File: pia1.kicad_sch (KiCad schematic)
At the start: 33 parts, among them IC20 MC14529B, IC24 74LS244N, IC25 LM393P, IC26 MC6821

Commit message: move to samx4
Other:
- company: (none) -> Dragon Data
- title: (none) -> Dragon 32 CPU UK PAL
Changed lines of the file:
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@@
   (paper "A3")
   (title_block
+    (title "Dragon 32 CPU UK PAL")
     (date "2023-05-25")
     (rev "3.0")
-    (comment 2 "Reposition dram and buffer")
+    (company "Dragon Data")
+    (comment 1 "Modified by Julian Brown")
+    (comment 2 "SAMx4 by Ciaran Anscomb")
   )
   (junction (at 89.281 73.406) (diameter 0) (color 0 0 0 0)

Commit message: rework board
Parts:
- removed IC26: MC6821, Package_DIP:DIP-40_W15.24mm, symbol Motorola PIA:MC6821
- added U5: W65C21, Package_LCC:PLCC-44_SMD-Socket, symbol Motorola PIA:W65C21
- C1, C38, C39, C43, C45, C68, C69: footprint Capacitor_THT:C_Disc_D4.3mm_W1.9mm_P5.00mm -> Capacitor_SMD:C_0805_2012Metric_Pad1.18x1.45mm_HandSolder
- C30, C31, C32, C33: footprint Capacitor_THT:C_Disc_D5.0mm_W2.5mm_P5.00mm -> Capacitor_SMD:C_0805_2012Metric_Pad1.18x1.45mm_HandSolder
- D8, D9: footprint Diode_THT:D_DO-35_SOD27_P7.62mm_Horizontal -> Diode_SMD:D_SOD-323_HandSoldering
- IC24: value 74LS244N -> 74ACT244N; footprint Package_DIP:DIP-20_W7.62mm -> Package_SO:SOIC-20W_7.5x12.8mm_P1.27mm; DigiKey 296-1653-5-ND -> 74ACT244SCXCT-ND
- L1, L2, L3, L4: footprint Inductor_THT:L_Axial_L7.0mm_D3.3mm_P5.08mm_Vertical_Fastron_MICC -> Inductor_SMD:L_1812_4532Metric_Pad1.30x3.40mm_HandSolder
- R1, R42, R43, R53, R54, R55: footprint Resistor_THT:R_Axial_DIN0207_L6.3mm_D2.5mm_P10.16mm_Horizontal -> Resistor_SMD:R_0805_2012Metric_Pad1.20x1.40mm_HandSolder
- R30, R31: footprint Resistor_THT:R_Axial_DIN0207_L6.3mm_D2.5mm_P2.54mm_Vertical -> Resistor_SMD:R_0805_2012Metric_Pad1.20x1.40mm_HandSolder
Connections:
- net +5V: now also U5.21 (VCC), U5.24 (CS0), U5.26 (CS1)
- net A0: now also U5.39 (RS0)
- net A1: now also U5.38 (RS1)
- net AD1: now also U5.43 (CA2)
- net AD2: now also U5.20 (CB2)
- net D0: now also U5.36 (D0)
- net D1: now also U5.35 (D1)
- net D2: now also U5.34 (D2)
- net D3: now also U5.33 (D3)
- net D4: now also U5.32 (D4)
- net D5: now also U5.31 (D5)
- net D6: now also U5.30 (D6)
- net D7: now also U5.29 (D7)
- net E: now also U5.28 (E)
- net GND: now also U5.1 (VSS)
- net P0: now also U5.25 (~{CS2})
- net PA0: now also U5.3 (PA0)
- net PA1: now also U5.4 (PA1)
- net PA2: now also U5.5 (PA2)
- net PA3: now also U5.6 (PA3)
- net PA4: now also U5.7 (PA4)
- net PA5: now also U5.8 (PA5)
- net PA6: now also U5.9 (PA6)
- net PA7: now also U5.10 (PA7)
- net PB0: now also U5.11 (PB0)
- net PB1: now also U5.12 (PB1)
- net PB2: now also U5.13 (PB2)
- net PB3: now also U5.14 (PB3)
- net PB4: now also U5.15 (PB4)
- net PB5: now also U5.16 (PB5)
- net PB6: now also U5.17 (PB6)
- net PB7: now also U5.18 (PB7)
- net R/~{W}: now also U5.23 (R/~{W})
- net ~{FS}: now also U5.19 (CB1)
- net ~{IRQ}: now also U5.41 (~{IRQB}), U5.42 (~{IRQA})
- net ~{NHS}: now also U5.44 (CA1)
- net ~{RES}: now also U5.37 (~{RESET})

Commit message: serial wiring
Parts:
- removed IC20: MC14529B, Package_DIP:DIP-16_W7.62mm, symbol Motorola PIA:MC14529B
- removed IC25: LM393P, Package_DIP:DIP-8_W7.62mm, symbol Comparator:LM393
- removed R53: 10M, Resistor_SMD:R_0805_2012Metric_Pad1.20x1.40mm_HandSolder, symbol Device:R_Small
- removed R54: 1K, Resistor_SMD:R_0805_2012Metric_Pad1.20x1.40mm_HandSolder, symbol Device:R_Small
- removed R55: 10K, Resistor_SMD:R_0805_2012Metric_Pad1.20x1.40mm_HandSolder, symbol Device:R_Small
- added IC1: LM393DR, Package_SO:SOP-8_3.9x4.9mm_P1.27mm, symbol Comparator:LM393
- added JP3: Serial, Jumper:SolderJumper-3_P1.3mm_Open_Pad1.0x1.5mm, symbol Jumper:SolderJumper_3_Open
- added R28: 4K7, Resistor_SMD:R_0805_2012Metric_Pad1.20x1.40mm_HandSolder, symbol Device:R_Small
- added R33: 10M, Resistor_SMD:R_0805_2012Metric_Pad1.20x1.40mm_HandSolder, symbol Device:R_Small
- added R34: 1K, Resistor_SMD:R_0805_2012Metric_Pad1.20x1.40mm_HandSolder, symbol Device:R_Small
- added U1: TS5A3166DBVR, Package_TO_SOT_SMD:SOT-23-5, symbol Analog_Switch:TS5A3166DBVR
- added U13: 4069, Package_SO:SOIC-14_3.9x8.7mm_P1.27mm, symbol 4xxx:4069
- added U2: 4052, Package_SO:TSSOP-16_4.4x5mm_P0.65mm, symbol 4xxx:4052
- R31: value 4K7 -> 10K; DigiKey CF14JT4K70CT-ND -> CF14JT10K0CT-ND
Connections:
- net +5V: now also JP3.3 (B), R28.2, R34.1, U1.5 (V+), U2.16 (VDD); no longer R31.2, U5.24 (CS0), U5.26 (CS1)
- net 6bit D/A: now also IC1.6 (_), U2.1 (Y0)
- net AD1: now also U2.10 (A)
- net AD2: now also U2.9 (B)
- net CASS: now also R28.1, U2.5 (Y1); no longer R31.1
- net CB2: now also U1.4
- net ESND: now also U2.2 (Y2)
- net GND: now also U1.3 (GND), U2.4 (Y3), U2.6 (Inh), U2.7 (VEE), U2.8 (VSS)
- net PA7: now also IC1.7, R33.1, R34.2
- net SOUND: now also U1.2
- net X0: now also U2.12 (X0)
- net X1: now also U2.14 (X1)
- net X2: now also U2.15 (X2)
- net X3: now also U2.11 (X3)
- new net: JP3.1 (A), U13.8
- new net: JP3.2 (C), U5.24 (CS0), U5.26 (CS1)
- new net: IC1.5 (+), R31.1, R33.2
- new net: U1.1, U2.3 (Y)
- new net: R31.2, U2.13 (X)
- new net A2: U13.9

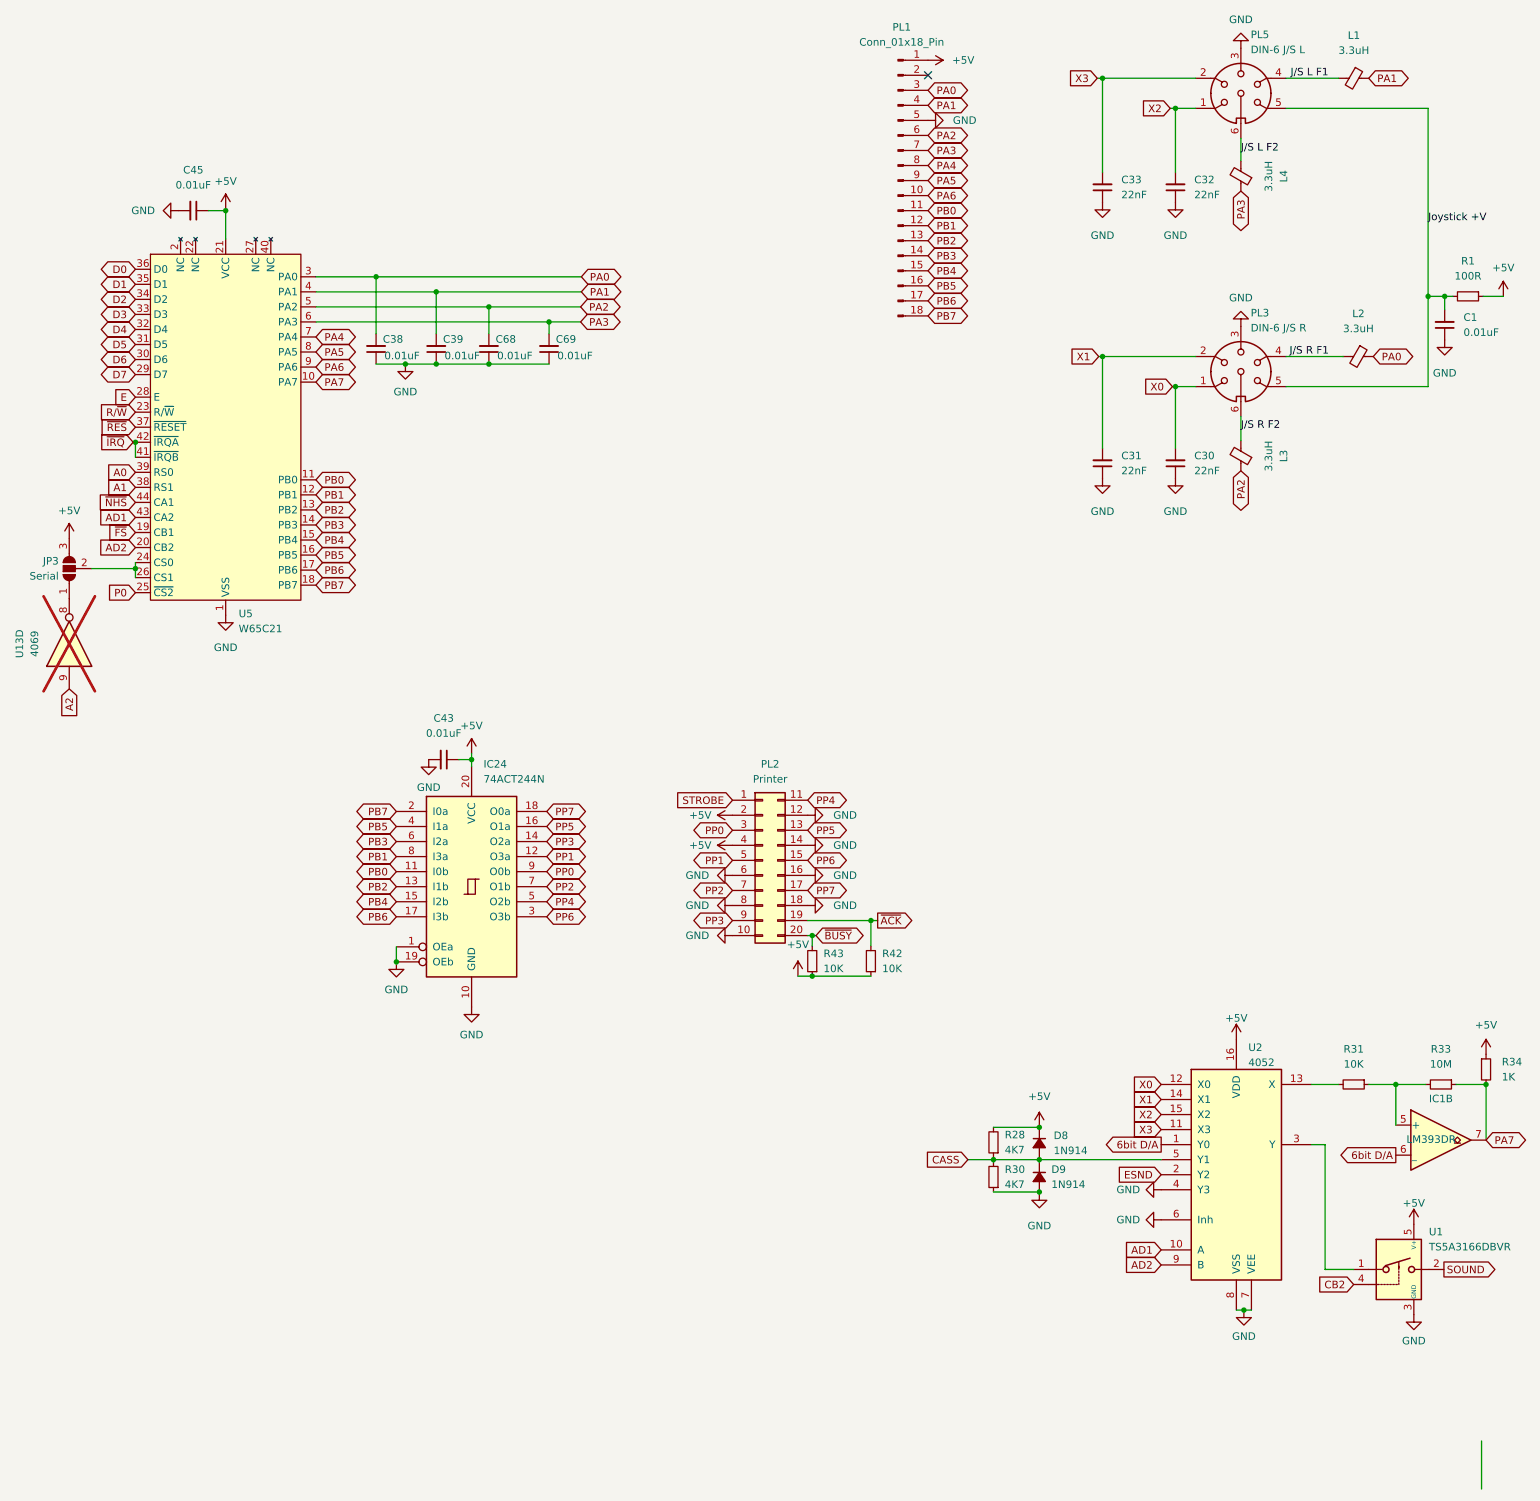
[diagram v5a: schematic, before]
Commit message: switch to fpga
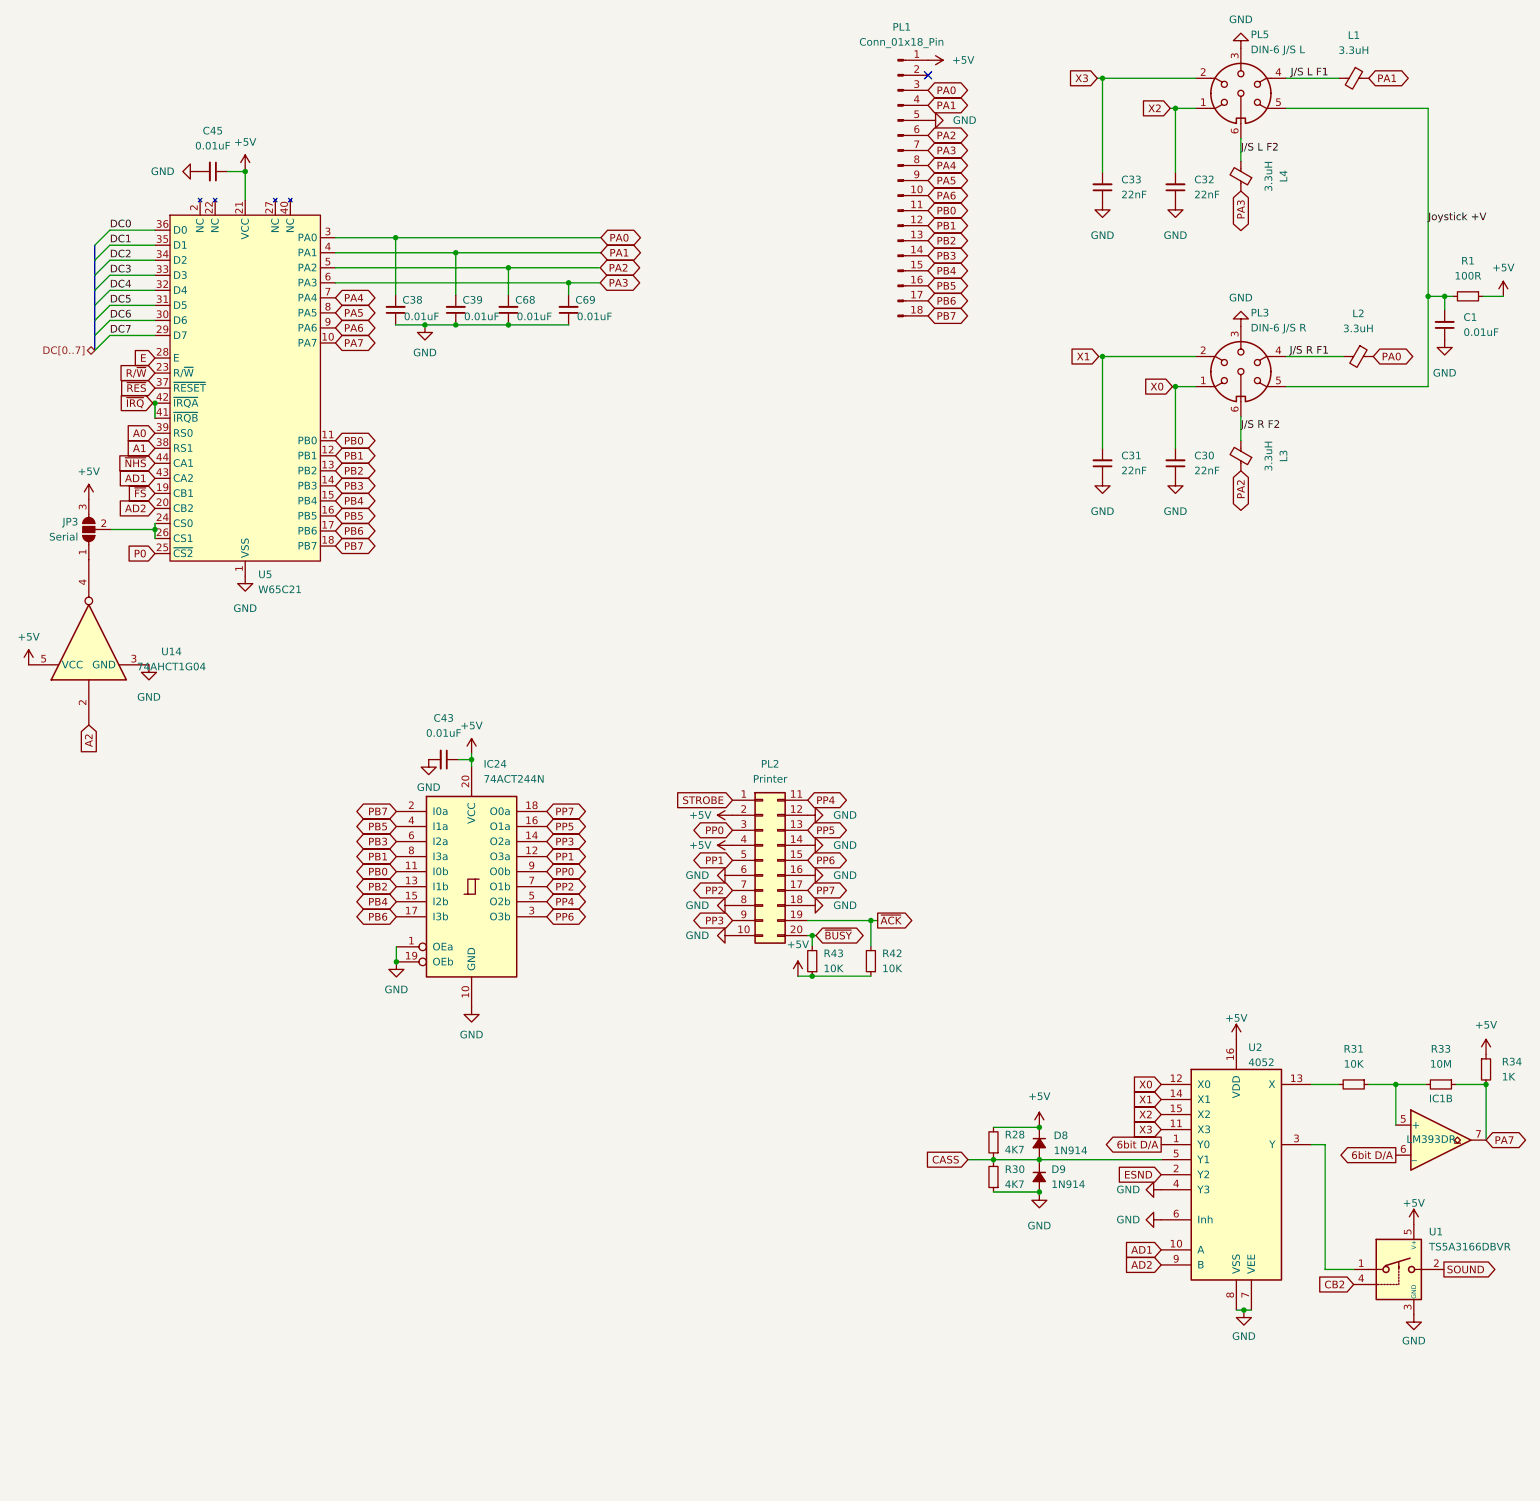
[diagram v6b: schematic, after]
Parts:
- removed U13: 4069, Package_SO:SOIC-14_3.9x8.7mm_P1.27mm, symbol 4xxx:4069
- added U14: 74AHCT1G04, Package_TO_SOT_SMD:SOT-23-5_HandSoldering, symbol 74xGxx:74AHCT1G04
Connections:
- net +5V: now also U14.5 (VCC)
- net A2: now also U14.2
- net GND: now also U14.3 (GND)
- net at JP3.1 (A): now also U14.4
- net D0 renamed DC0
- net D1 renamed DC1
- net D2 renamed DC2
- net D3 renamed DC3
- net D4 renamed DC4
- net D5 renamed DC5
- net D6 renamed DC6
- net D7 renamed DC7
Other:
- moved on the sheet: C38, C39, C45, C68, C69, JP3, U5

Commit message: rework traces for FPGA
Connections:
- net ~{IRQ} renamed ~{IRQx}
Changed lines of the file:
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@@
-	)
-	(junction
-		(at 46.99 80.01)
-		(diameter 0)
-		(color 0 0 0 0)
 	)
 	(junction
@@
 		)
 	)
+	(global_label "~{IRQx}"
+		(shape input)
+		(at 46.609 80.01 180)
+		(fields_autoplaced yes)
+		(effects
+			(font
+				(size 1.27 1.27)
+			)
+			(justify right)
+		)
+		(property "Intersheetrefs" "${INTERSHEET_REFS}"
+			(at 40.0446 80.01 0)
+			(effects
+				(font
+					(size 1.27 1.27)
+				)
+				(justify right)
+				(hide yes)
+			)
+		)
+	)
 	(global_label "PB5"
 		(shape bidirectional)
@@
 			(effects
 				(font
-					(size 1.27 1.27)
-				)
-				(justify right)
-				(hide yes)
-			)
-		)
-	)
-	(global_label "~{IRQ}"
-		(shape input)
-		(at 46.609 80.01 180)
-		(fields_autoplaced yes)
-		(effects
-			(font
-				(size 1.27 1.27)
-			)
-			(justify right)
-		)
-		(property "Intersheetrefs" "${INTERSHEET_REFS}"
-			(at 41.0796 79.9306 0)
-			(effects
-				(font
